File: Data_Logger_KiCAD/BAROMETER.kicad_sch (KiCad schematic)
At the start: 6 parts

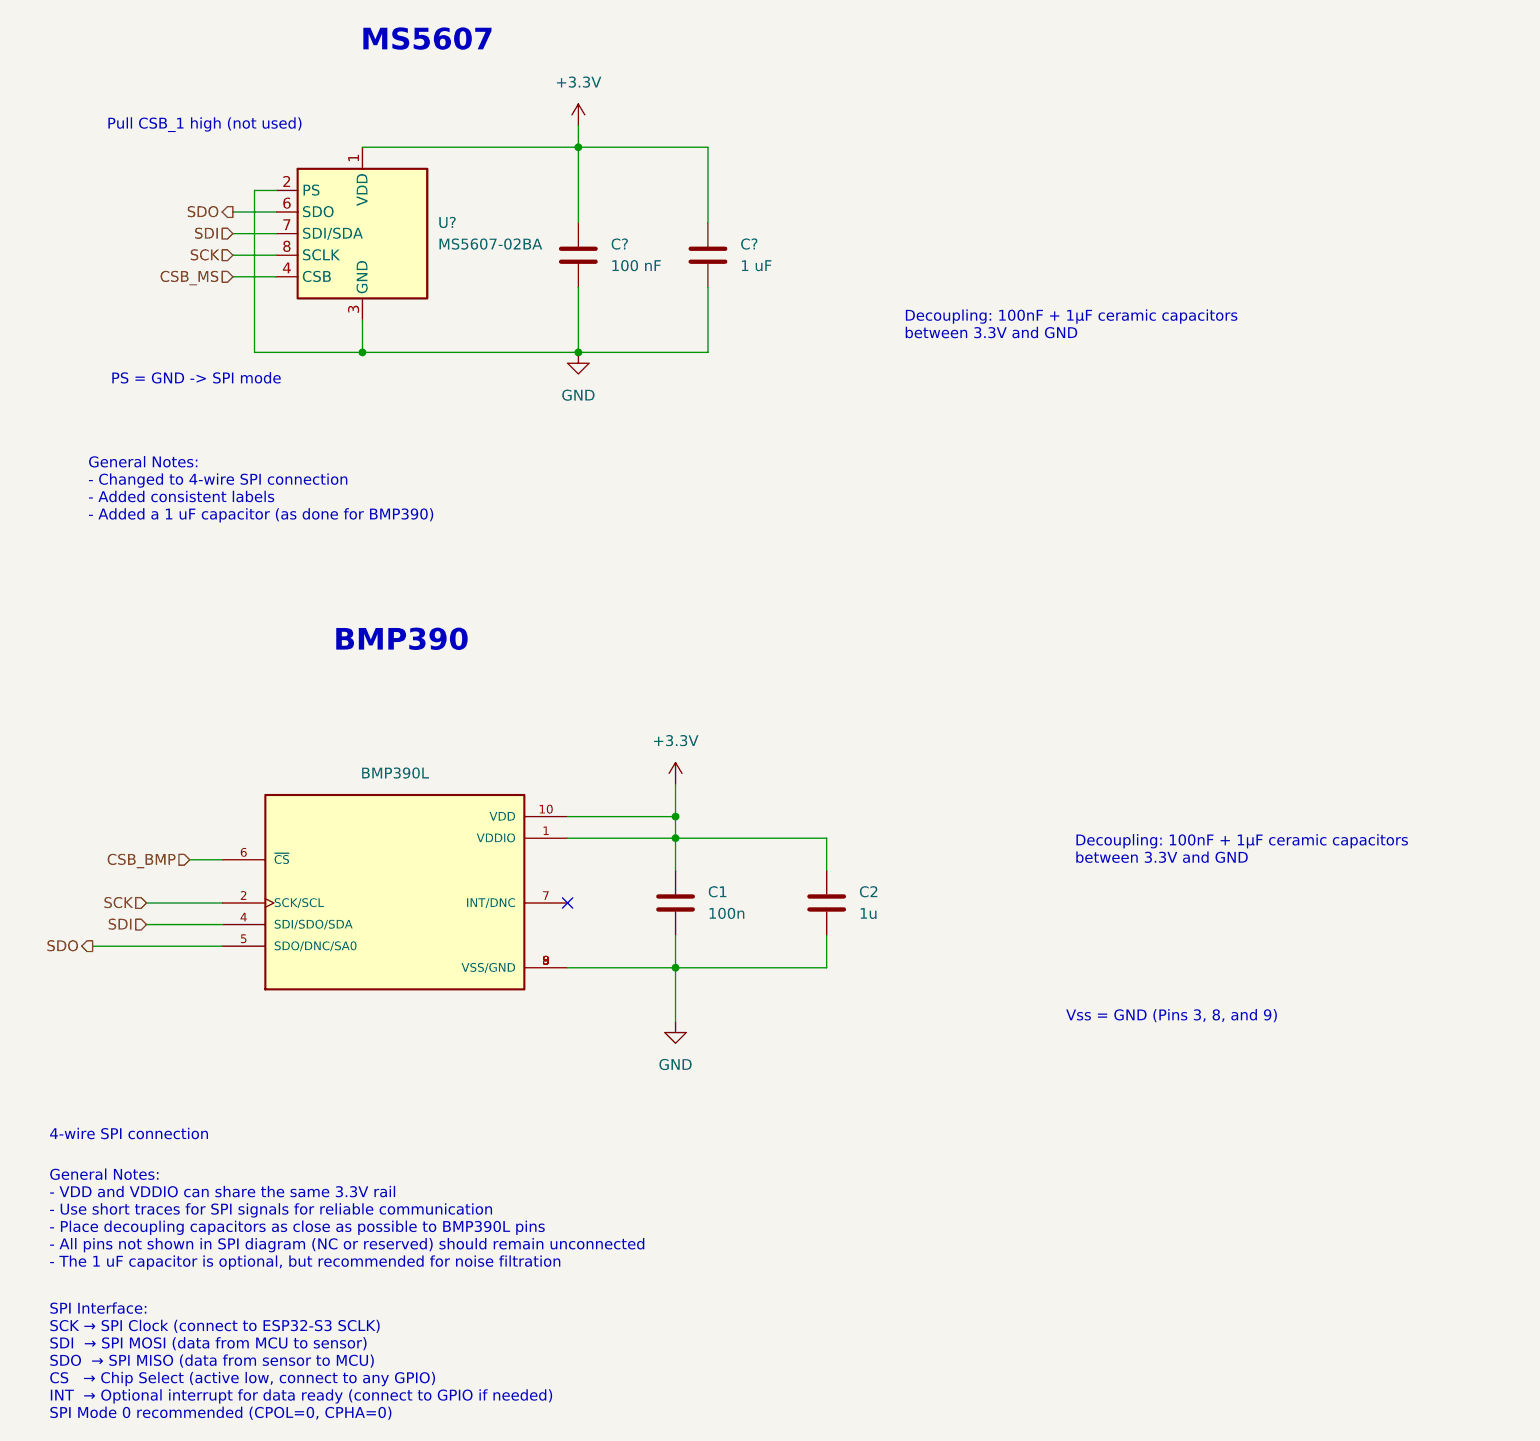
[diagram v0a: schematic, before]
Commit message: add footprint/LCSC to parts
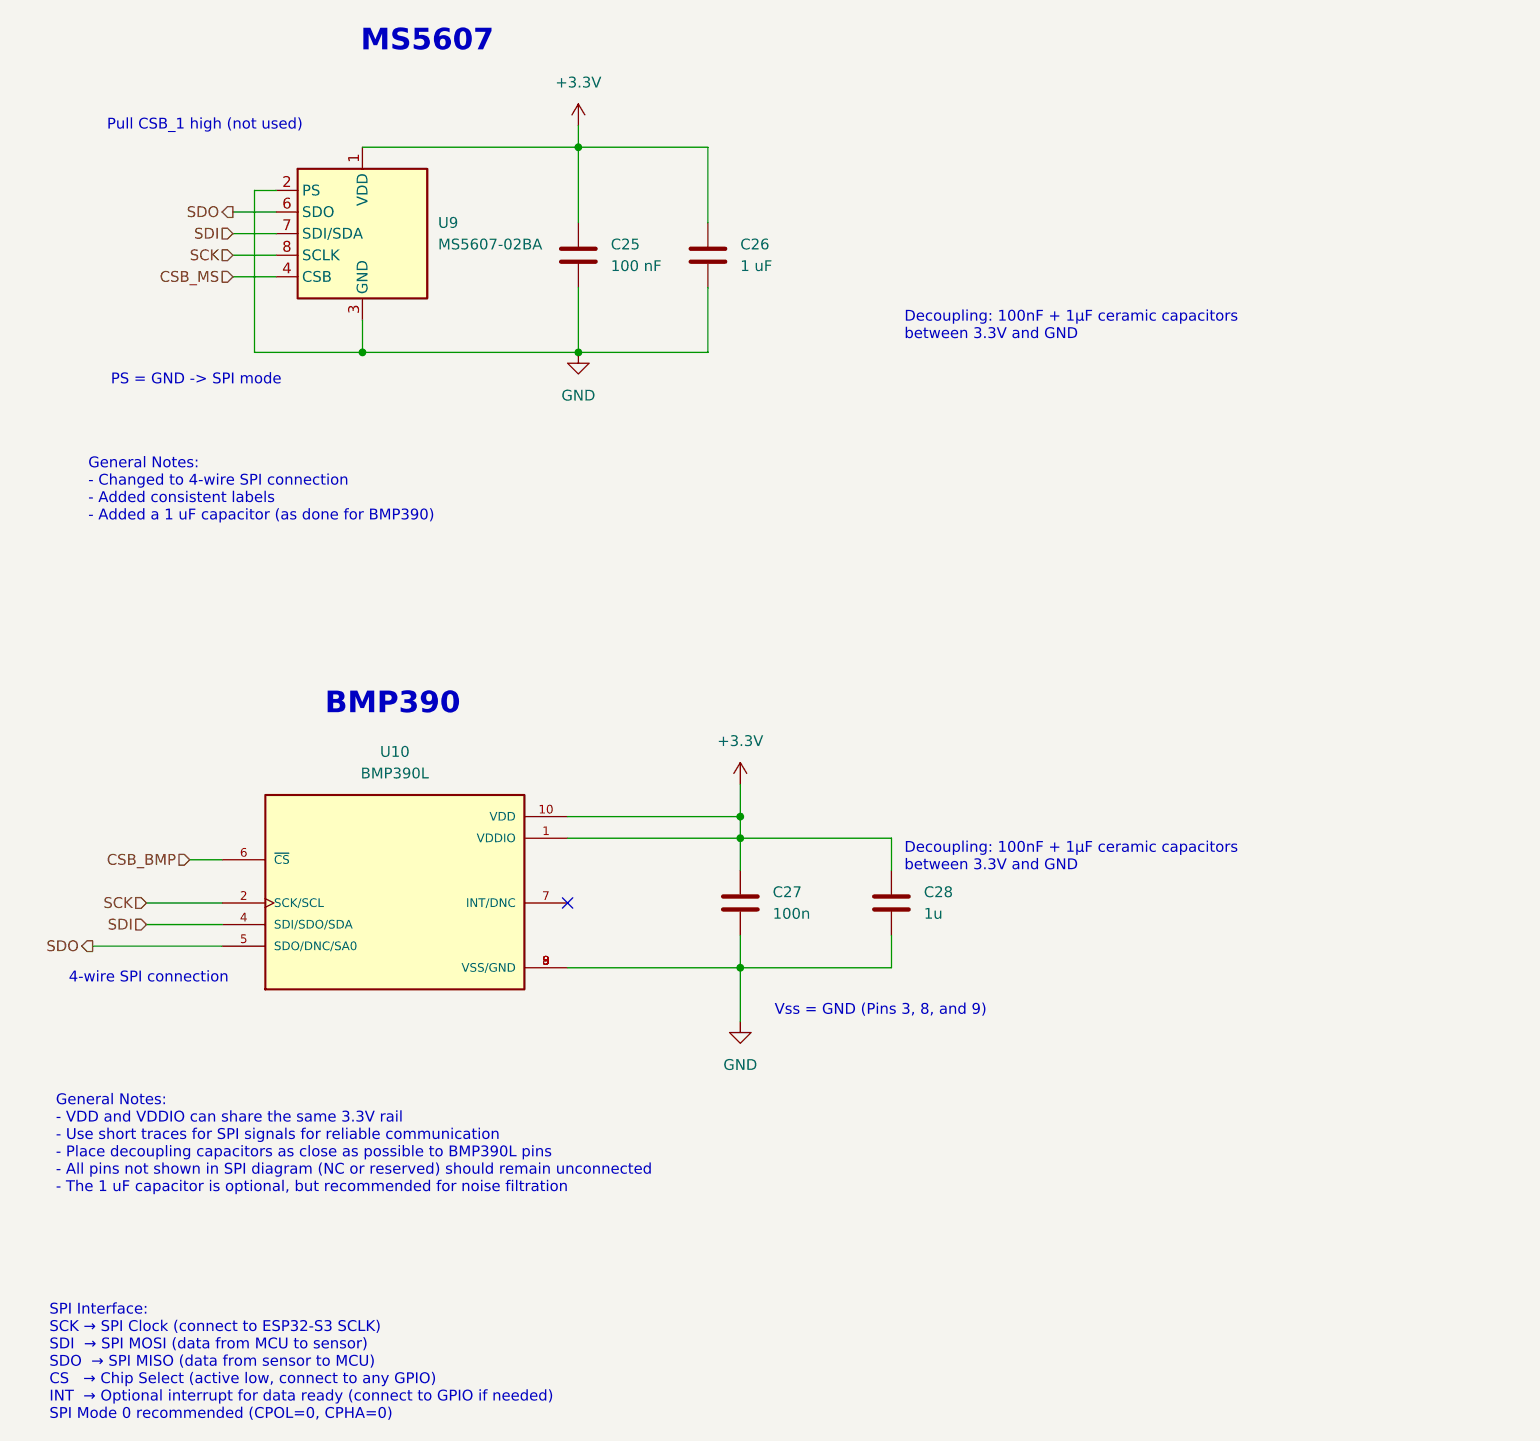
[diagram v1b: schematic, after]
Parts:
- gave numbers to parts that had none: 4
- renumbered C1 to C27, C2 to C28
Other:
- moved on the sheet: C27, C28

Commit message: minor updates
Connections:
- net CSB_BMP renamed ~{CSB_BMP}
- net CSB_MS renamed ~{CSB_MS}
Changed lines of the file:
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@@
 		)
 	)
-	(hierarchical_label "CSB_BMP"
+	(hierarchical_label "~{CSB_BMP}"
 		(shape input)
 		(at 40.64 116.84 180)
@@
 		)
 	)
-	(hierarchical_label "CSB_MS"
+	(hierarchical_label "~{CSB_MS}"
 		(shape input)
 		(at 45.72 48.26 180)

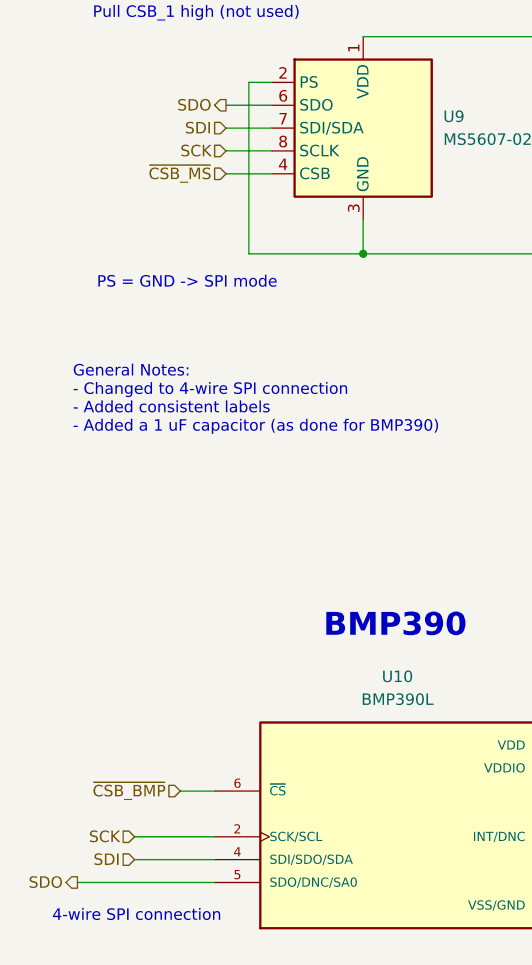
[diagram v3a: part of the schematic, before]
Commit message: rem old files and add LCSC #'s
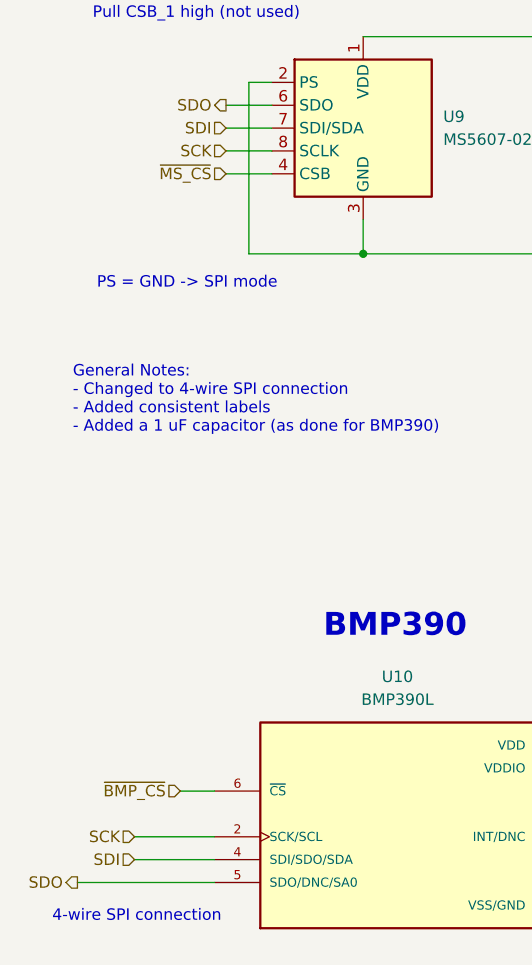
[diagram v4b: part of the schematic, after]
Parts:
- C25, C27: LCSC (none) -> C1525
- C26, C28: LCSC (none) -> C52923
- U9: LCSC (none) -> C97627
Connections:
- net ~{CSB_BMP} renamed ~{BMP_CS}
- net ~{CSB_MS} renamed ~{MS_CS}
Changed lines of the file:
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@@
 		)
 	)
-	(hierarchical_label "~{CSB_BMP}"
+	(hierarchical_label "~{BMP_CS}"
 		(shape input)
 		(at 40.64 116.84 180)
@@
 		)
 	)
-	(hierarchical_label "~{CSB_MS}"
+	(hierarchical_label "~{MS_CS}"
 		(shape input)
 		(at 45.72 48.26 180)
@@
 			)
 		)
+		(property "LCSC" "C1525"
+			(at 105.41 121.92 0)
+			(effects
+				(font
+					(size 1.27 1.27)
+				)
+				(hide yes)
+			)
+		)
 		(pin "1"
 		)
@@
 			)
 		)
+		(property "LCSC" "C52923"
+			(at 123.19 121.92 0)
+			(effects
+				(font
+					(size 1.27 1.27)
+				)
+				(hide yes)
+			)
+		)
 		(pin "1"
 		)
@@
 			)
 		)
+		(property "LCSC" "C1525"
+			(at 86.36 45.72 0)
+			(effects
+				(font
+					(size 1.27 1.27)
+				)
+				(hide yes)
+			)
+		)
 		(pin "1"
 		)
@@
 			)
 		)
+		(property "LCSC" "C52923"
+			(at 101.6 45.72 0)
+			(effects
+				(font
+					(size 1.27 1.27)
+				)
+				(hide yes)
+			)
+		)
 		(pin "1"
 		)
@@
 			(at 60.96 43.18 0)
 			(effects
+				(font
+					(size 1.27 1.27)
+				)
+				(hide yes)
+			)
+		)
+		(property "LCSC" "C97627"
+			(at 60.96 43.18 0)
+			(effects

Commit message: fix footprint errors
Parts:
- U10: footprint BMP390L:XDCR_BMP390L -> custom:XDCR_BMP390L
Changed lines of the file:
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@@
 			)
 		)
-		(property "Footprint" "BMP390L:XDCR_BMP390L"
+		(property "Footprint" "custom:XDCR_BMP390L"
 			(at 64.77 121.92 0)
 			(effects

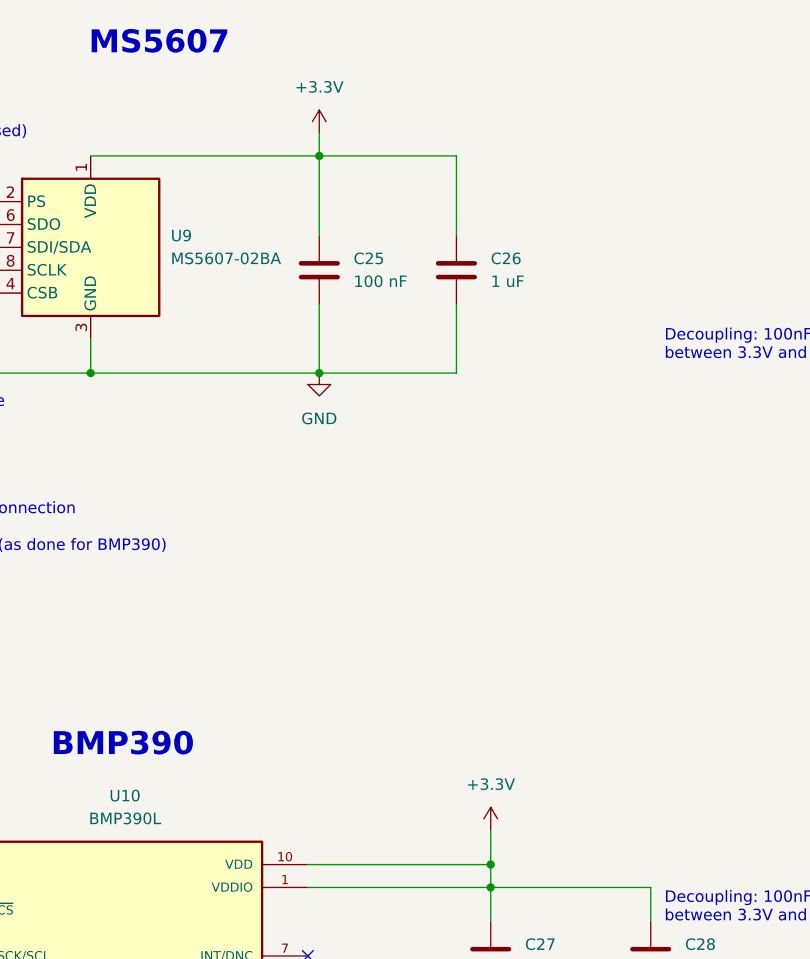
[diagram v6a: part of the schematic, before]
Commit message: layout power plane
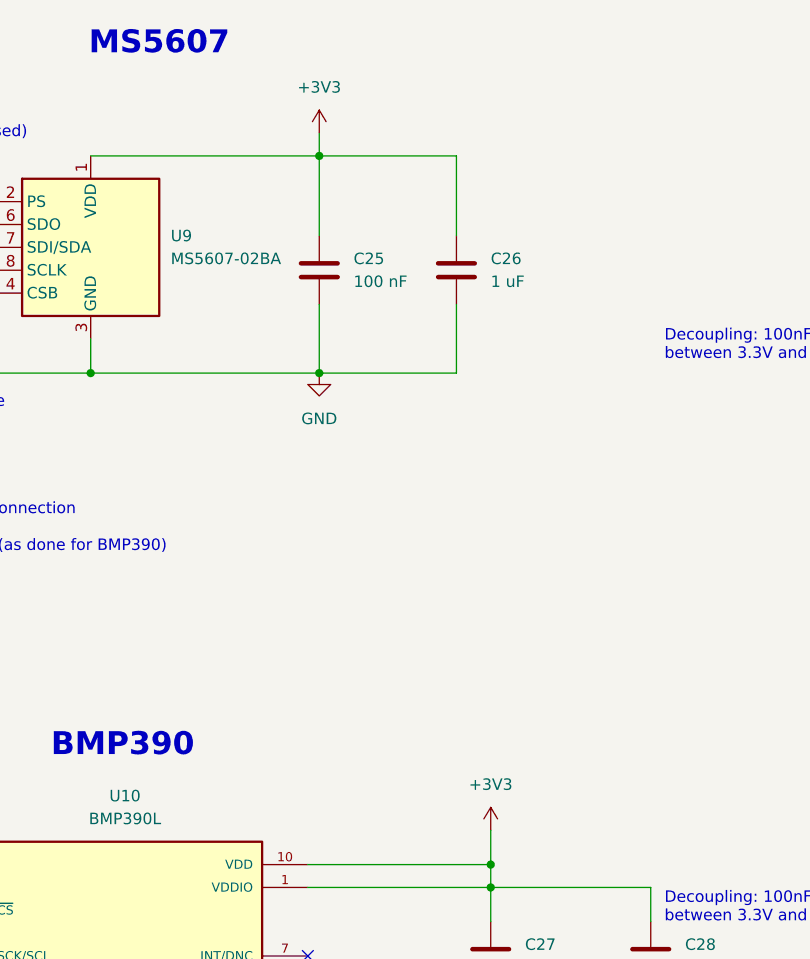
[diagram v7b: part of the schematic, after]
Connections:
- net +3.3V renamed +3V3
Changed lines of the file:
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@@
-	)
-	(symbol
-		(lib_id "power:+3.3V")
-		(at 86.36 30.48 0)
-		(unit 1)
-		(exclude_from_sim no)
-		(in_bom yes)
-		(on_board yes)
-		(dnp no)
-		(property "Reference" "#PWR046"
-			(at 86.36 34.29 0)
-			(effects
-				(font
-					(size 1.27 1.27)
-				)
-				(hide yes)
-			)
-		)
-		(property "Value" "+3.3V"
-			(at 86.36 25.4 0)
-			(effects
-				(font
-					(size 1.27 1.27)
-				)
-			)
-		)
-		(property "Footprint" ""
-			(at 86.36 30.48 0)
-			(effects
-				(font
-					(size 1.27 1.27)
-				)
-				(hide yes)
-			)
-		)
-		(property "Datasheet" ""
-			(at 86.36 30.48 0)
-			(effects
-				(font
-					(size 1.27 1.27)
-				)
-				(hide yes)
-			)
-		)
-		(property "Description" "Power symbol creates a global label with name \"+3.3V\""
-			(at 86.36 30.48 0)
-			(effects
-				(font
-					(size 1.27 1.27)
-				)
-				(hide yes)
-			)
-		)
-		(pin "1"
-		)
-		(instances
-			(project "Data_Logger_Board"
-				(path "/db968e42-3ace-4cc9-9096-9d8f48135c40/795ab2be-9db7-4254-b05c-ac2b60177344/909dd632-2a0f-4e55-b8e6-044af71dac19"
-					(reference "#PWR046")
-					(unit 1)
-				)
-			)
-		)
 	)
 	(symbol
@@
 	)
 	(symbol
+		(lib_id "power:+3V3")
+		(at 105.41 107.95 0)
+		(unit 1)
+		(exclude_from_sim no)
+		(in_bom yes)
+		(on_board yes)
+		(dnp no)
+		(fields_autoplaced yes)
+		(property "Reference" "#PWR046"
+			(at 105.41 111.76 0)
+			(effects
+				(font
+					(size 1.27 1.27)
+				)
+				(hide yes)
+			)
+		)
+		(property "Value" "+3V3"
+			(at 105.41 102.87 0)
+			(effects
+				(font
+					(size 1.27 1.27)
+				)
+			)
+		)
+		(property "Footprint" ""
+			(at 105.41 107.95 0)
+			(effects
+				(font
+					(size 1.27 1.27)
+				)
+				(hide yes)
+			)
+		)
+		(property "Datasheet" ""
+			(at 105.41 107.95 0)
+			(effects
+				(font
+					(size 1.27 1.27)
+				)
+				(hide yes)
+			)
+		)
+		(property "Description" "Power symbol creates a global label with name \"+3V3\""
+			(at 105.41 107.95 0)
+			(effects
+				(font
+					(size 1.27 1.27)
+				)
+				(hide yes)
+			)
+		)
+		(pin "1"
+		)
+		(instances
+			(project ""
+				(path "/db968e42-3ace-4cc9-9096-9d8f48135c40/795ab2be-9db7-4254-b05c-ac2b60177344/909dd632-2a0f-4e55-b8e6-044af71dac19"
+					(reference "#PWR046")
+					(unit 1)
+				)
+			)
+		)
+	)
+	(symbol
 		(lib_id "Device:C")
 		(at 86.36 45.72 0)
@@
 	)
 	(symbol
-		(lib_id "power:+3.3V")
-		(at 105.41 107.95 0)
+		(lib_id "power:+3V3")
+		(at 86.36 30.48 0)
 		(unit 1)
 		(exclude_from_sim no)
@@
 		(dnp no)
 		(fields_autoplaced yes)
-		(property "Reference" "#PWR048"
-			(at 105.41 111.76 0)
-			(effects
-				(font
-					(size 1.27 1.27)
-				)
-				(hide yes)
-			)
-		)
-		(property "Value" "+3.3V"
-			(at 105.41 102.87 0)
+		(property "Reference" "#PWR034"
+			(at 86.36 34.29 0)
+			(effects
+				(font
+					(size 1.27 1.27)
+				)
+				(hide yes)
+			)
+		)
+		(property "Value" "+3V3"
+			(at 86.36 25.4 0)
 			(effects
 				(font
@@
 		)
 		(property "Footprint" ""
-			(at 105.41 107.95 0)
+			(at 86.36 30.48 0)
 			(effects
 				(font
@@
 		)
 		(property "Datasheet" ""
-			(at 105.41 107.95 0)
-			(effects
-				(font
-					(size 1.27 1.27)
-				)
-				(hide yes)
-			)
-		)
-		(property "Description" "Power symbol creates a global label with name \"+3.3V\""
-			(at 105.41 107.95 0)
-			(effects
-				(font
-					(size 1.27 1.27)
-				)
-				(hide yes)
-			)
-		)
-		(pin "1"
-		)
-		(instances
-			(project "Data_Logger_Board"
-				(path "/db968e42-3ace-4cc9-9096-9d8f48135c40/795ab2be-9db7-4254-b05c-ac2b60177344/909dd632-2a0f-4e55-b8e6-044af71dac19"
-					(reference "#PWR048")
-					(unit 1)
-				)
+			(at 86.36 30.48 0)
+			(effects
+				(font
+					(size 1.27 1.27)
+				)
+				(hide yes)
+			)
+		)
+		(property "Description" "Power symbol creates a global label with name \"+3V3\""
+			(at 86.36 30.48 0)
+			(effects
+				(font
+					(size 1.27 1.27)
+				)
+				(hide yes)
+			)
+		)
+		(pin "1"
+		)
+		(instances
+			(project ""
+				(path "/db968e42-3ace-4cc9-9096-9d8f48135c40/795ab2be-9db7-4254-b05c-ac2b60177344/909dd632-2a0f-4e55-b8e6-044af71dac19"
+					(reference "#PWR034")
+					(unit 1)
+				)

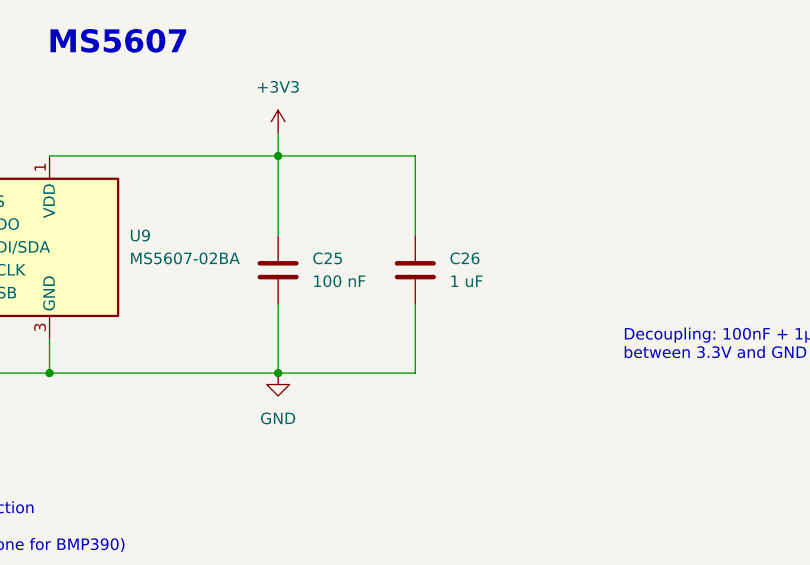
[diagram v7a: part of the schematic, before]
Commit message: remove units for extraction
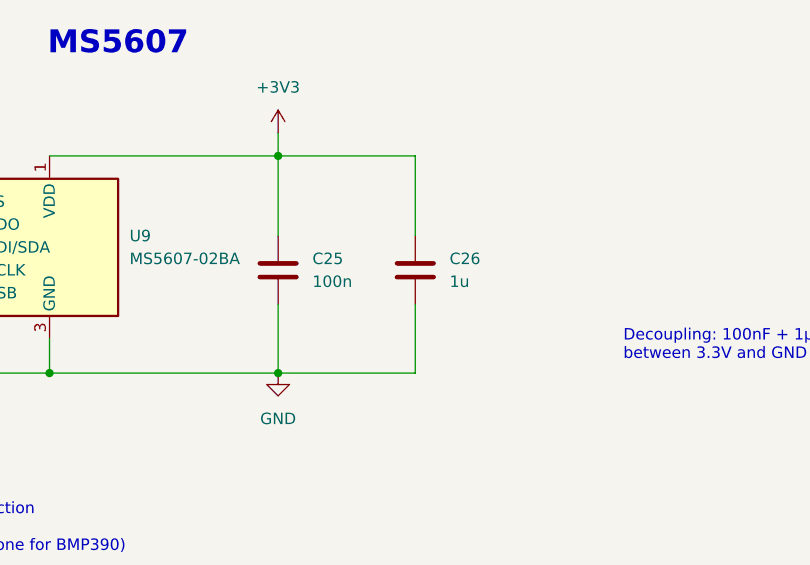
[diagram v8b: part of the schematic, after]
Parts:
- C25: value 100 nF -> 100n
- C26: value 1 uF -> 1u
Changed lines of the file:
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@@
 			)
 		)
-		(property "Value" "100 nF"
+		(property "Value" "100n"
 			(at 90.17 46.9899 0)
 			(effects
@@
 			)
 		)
-		(property "Value" "1 uF"
+		(property "Value" "1u"
 			(at 105.41 46.9899 0)
 			(effects
